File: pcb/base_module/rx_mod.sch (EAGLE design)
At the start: 29 parts, among them IC1 OPA336N, U1 ATMEGA328

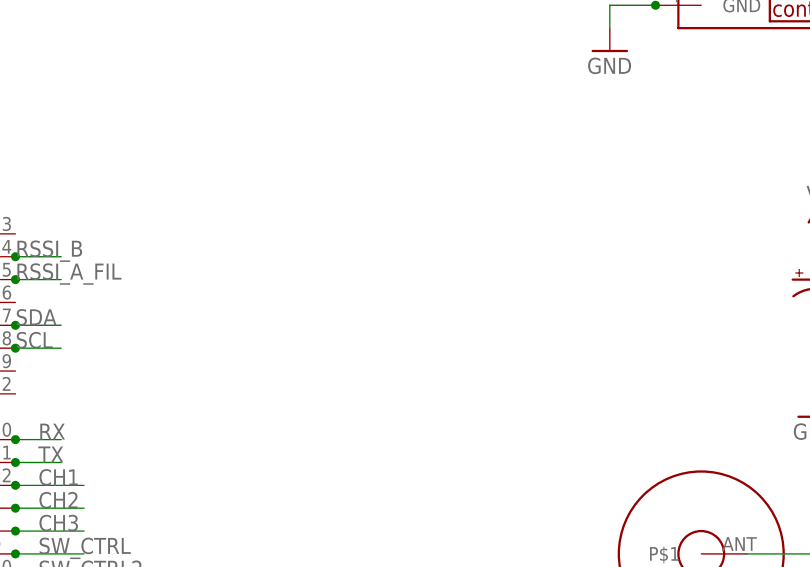
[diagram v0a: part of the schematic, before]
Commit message: new V4.1 base module (I2C OLED pins exposed + some bug fix)
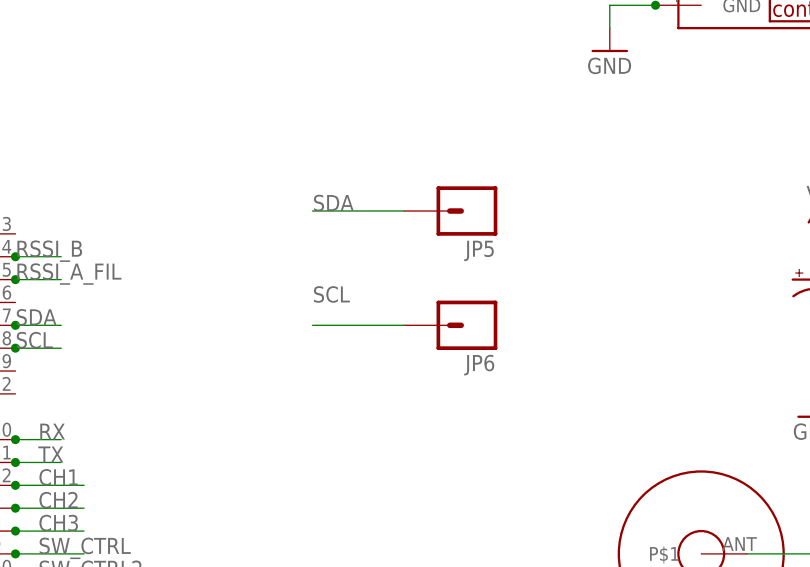
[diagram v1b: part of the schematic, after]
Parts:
- added JP5, JP6: (no value), SparkFun-Connectors:M01SMD-4.5X1.5
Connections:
- net SCL: now also JP6.1
- net SDA: now also JP5.1
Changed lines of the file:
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@@
 <?xml version="1.0" encoding="utf-8"?>
 <!DOCTYPE eagle SYSTEM "eagle.dtd">
-<eagle version="7.5.0">
+<eagle version="7.7.0">
 <drawing>
 <settings>
@@
 <part name="P+5" library="SparkFun" deviceset="3.3V" device="" value="VCC"/>
 <part name="SJ1" library="jumper" deviceset="SJ" device=""/>
+<part name="JP5" library="SparkFun-Connectors" deviceset="M01" device="SMD-4.5X1.5"/>
+<part name="JP6" library="SparkFun-Connectors" deviceset="M01" device="SMD-4.5X1.5"/>
 </parts>
 <sheets>
@@
 <instance part="P+5" gate="G$1" x="15.24" y="157.48"/>
 <instance part="SJ1" gate="1" x="10.16" y="114.3"/>
+<instance part="JP5" gate="G$1" x="157.48" y="86.36" rot="R180"/>
+<instance part="JP6" gate="G$1" x="157.48" y="73.66" rot="R180"/>
 </instances>
 <busses>
@@
 <junction x="106.68" y="71.12"/>
 </segment>
+<segment>
+<pinref part="JP6" gate="G$1" pin="1"/>
+<wire x1="149.86" y1="73.66" x2="139.7" y2="73.66" width="0.1524" layer="91"/>
+<label x="139.7" y="76.2" size="1.778" layer="95"/>
+</segment>
 </net>
 <net name="SDA" class="0">
@@
 <junction x="106.68" y="73.66"/>
 </segment>
-</net>
+<segment>
+<pinref part="JP5" gate="G$1" pin="1"/>
+<wire x1="149.86" y1="86.36" x2="139.7" y2="86.36" width="0.1524" layer="91"/>
+<label x="139.7" y="86.36" size="1.778" layer="95"/>
+</segment>
+</net>
